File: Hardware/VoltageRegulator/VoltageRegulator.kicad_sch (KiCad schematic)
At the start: 9 parts, among them J1 Conn_01x04, U1 TPS7A2501DRVR

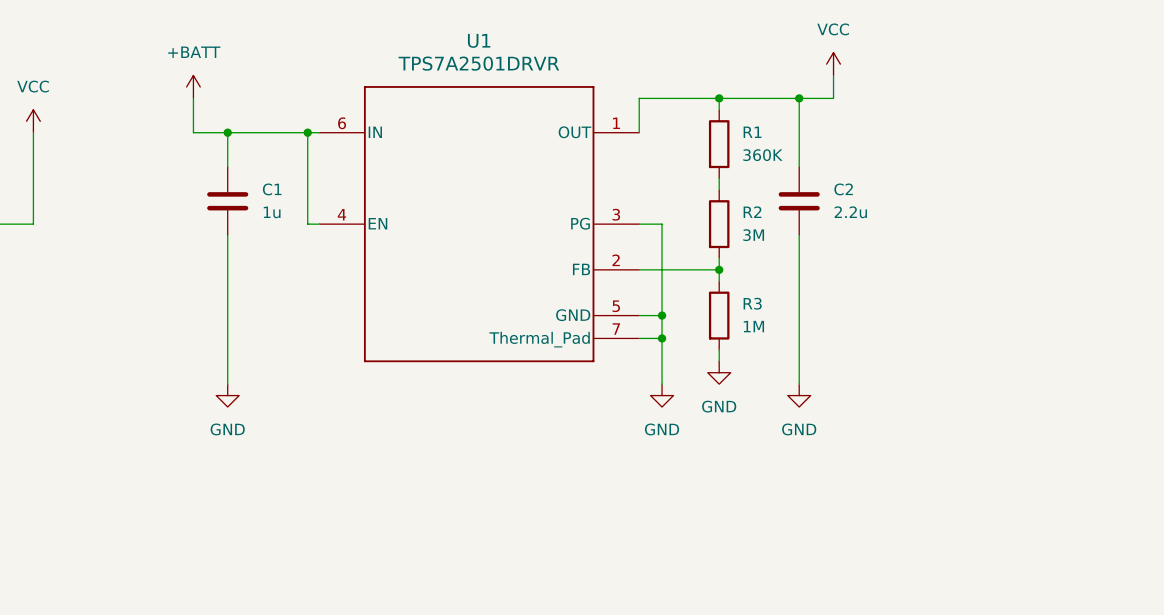
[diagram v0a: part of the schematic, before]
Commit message: Smaller board with isolated mounting holes
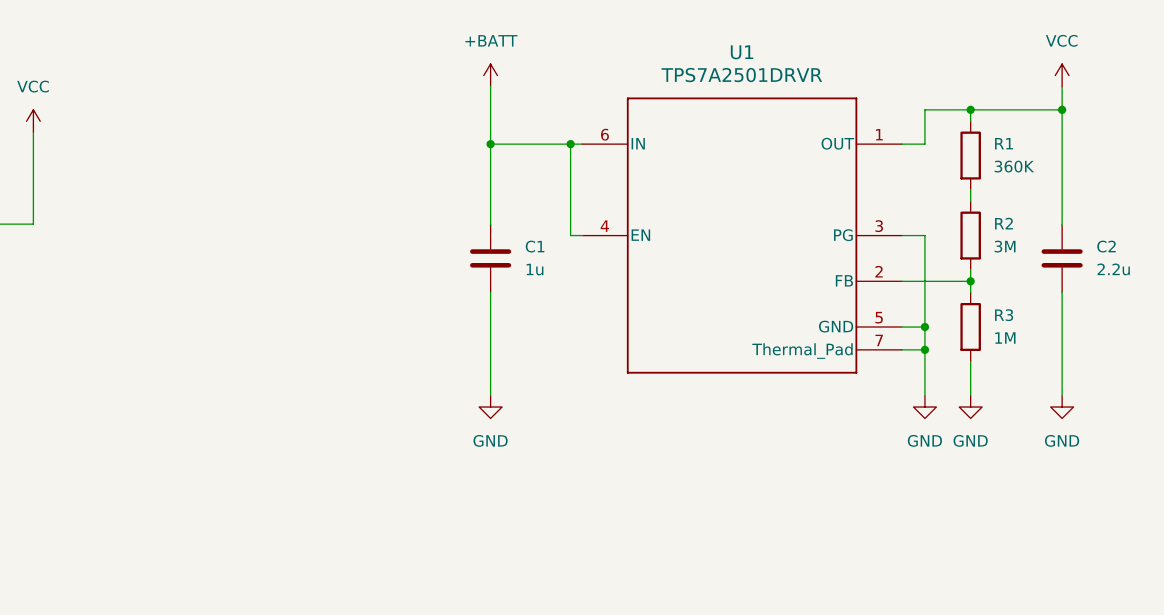
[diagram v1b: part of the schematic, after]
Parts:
- H1, H2: footprint MountingHole:MountingHole_3.2mm_M3 -> MountingHole:MountingHole_3.5mm
- U1: footprint TPS7A2501:DRV0006A-MFG -> TPS7A2501:DRV0006A-IPC_C
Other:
- company: (none) -> Clough42 LLC
- title: (none) -> Mercury Battery Replacement
- moved on the sheet: C1, C2, R1, R2, R3, U1

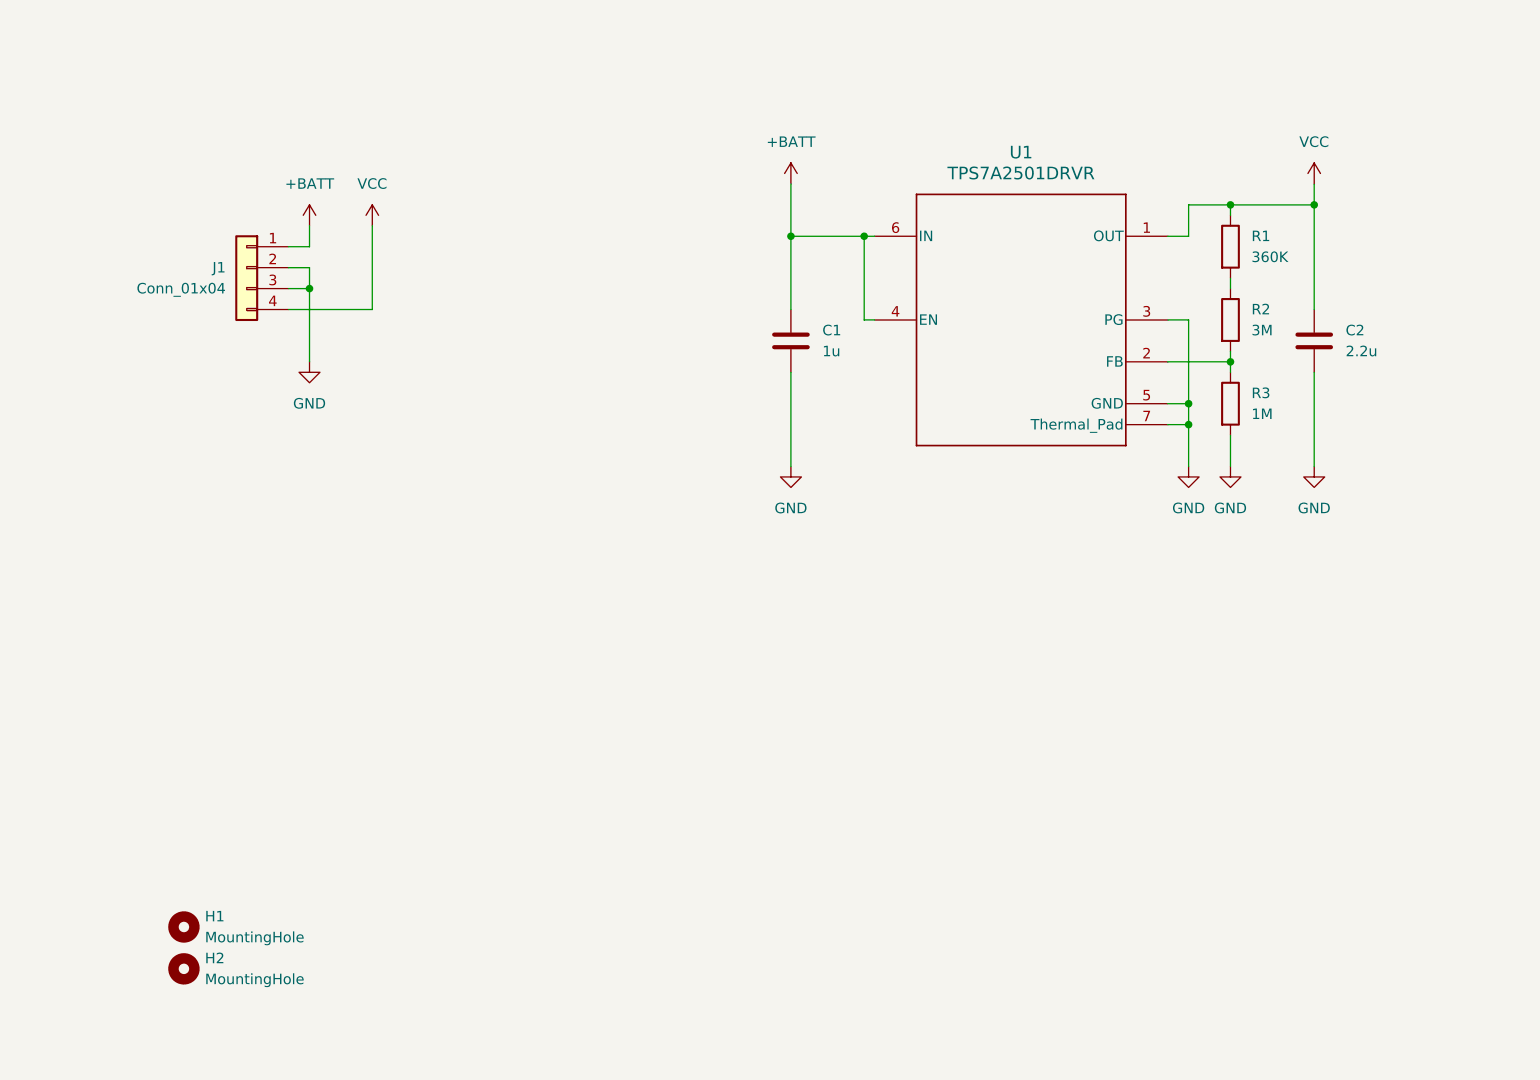
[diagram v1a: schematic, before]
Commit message: Neaten up schematic, add precision designators for resistors
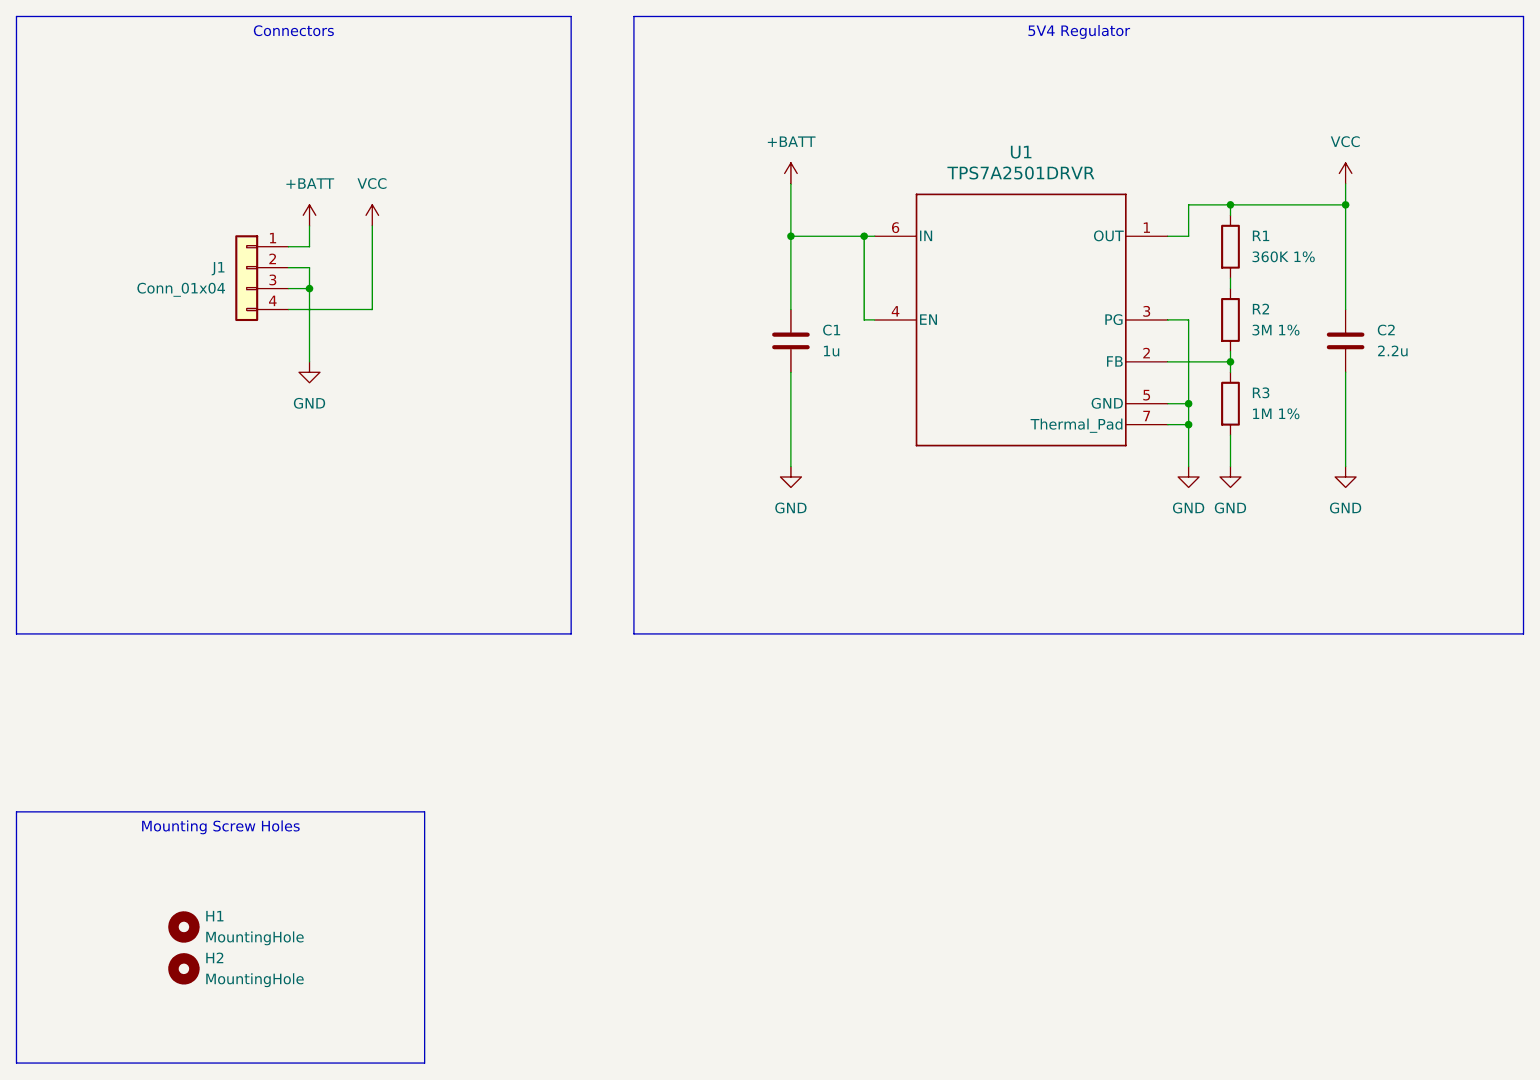
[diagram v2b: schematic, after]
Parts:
- R1: value 360K -> 360K 1%
- R2: value 3M -> 3M 1%
- R3: value 1M -> 1M 1%
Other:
- moved on the sheet: C2
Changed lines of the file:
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@@
     (comment 2 "Low dropout, ultra-low quiescent current")
   )
-  (junction (at 203.2 74.93) (diameter 0) (color 0 0 0 0)
-  )
   (junction (at 193.04 74.93) (diameter 0) (color 0 0 0 0)
   )
@@
   (junction (at 139.7 78.74) (diameter 0) (color 0 0 0 0)
   )
+  (junction (at 207.01 74.93) (diameter 0) (color 0 0 0 0)
+  )
   (wire (pts (xy 185.42 101.6) (xy 187.96 101.6))
     (stroke (width 0) (type default))
@@
     (stroke (width 0) (type default))
   )
-  (wire (pts (xy 193.04 74.93) (xy 203.2 74.93))
-    (stroke (width 0) (type default))
-  )
   (wire (pts (xy 88.9 87.63) (xy 88.9 77.47))
     (stroke (width 0) (type default))
   )
-  (wire (pts (xy 203.2 74.93) (xy 203.2 72.39))
+  (wire (pts (xy 207.01 74.93) (xy 207.01 72.39))
     (stroke (width 0) (type default))
   )
@@
     (stroke (width 0) (type default))
   )
-  (wire (pts (xy 203.2 95.25) (xy 203.2 106.68))
-    (stroke (width 0) (type default))
-  )
   (wire (pts (xy 187.96 74.93) (xy 193.04 74.93))
     (stroke (width 0) (type default))
@@
     (stroke (width 0) (type default))
   )
+  (wire (pts (xy 193.04 74.93) (xy 207.01 74.93))
+    (stroke (width 0) (type default))
+  )
   (wire (pts (xy 185.42 88.9) (xy 187.96 88.9))
     (stroke (width 0) (type default))
@@
     (stroke (width 0) (type default))
   )
-  (wire (pts (xy 203.2 74.93) (xy 203.2 87.63))
+  (wire (pts (xy 207.01 74.93) (xy 207.01 87.63))
     (stroke (width 0) (type default))
   )
@@
     (stroke (width 0) (type default))
   )
+  (wire (pts (xy 207.01 95.25) (xy 207.01 106.68))
+    (stroke (width 0) (type default))
+  )
   (wire (pts (xy 78.74 87.63) (xy 88.9 87.63))
     (stroke (width 0) (type default))
@@
     (stroke (width 0) (type default))
   )
+  (text_box "5V4 Regulator"
+    (at 120.65 52.07 0) (size 107.95 74.93)
+    (stroke (width 0) (type default))
+    (fill (type none))
+    (effects (font (size 1.27 1.27)) (justify top))
+  )
+  (text_box "Mounting Screw Holes"
+    (at 45.72 148.59 0) (size 49.53 30.48)
+    (stroke (width 0) (type default))
+    (fill (type none))
+    (effects (font (size 1.27 1.27)) (justify top))
+  )
+  (text_box "Connectors"
+    (at 45.72 52.07 0) (size 67.31 74.93)
+    (stroke (width 0) (type default))
+    (fill (type none))
+    (effects (font (size 1.27 1.27)) (justify top))
+  )
   (symbol (lib_id "Device:R") (at 193.04 88.9 0) (unit 1)
     (in_bom yes) (on_board yes) (dnp no) (fields_autoplaced)
@@
       (effects (font (size 1.27 1.27)) (justify left))
     )
-    (property "Value" "3M" (at 195.58 90.17 0)
+    (property "Value" "3M 1%" (at 195.58 90.17 0)
       (effects (font (size 1.27 1.27)) (justify left))
     )
@@
     )
   )
-  (symbol (lib_id "power:GND") (at 203.2 106.68 0) (unit 1)
-    (in_bom yes) (on_board yes) (dnp no) (fields_autoplaced)
-    (property "Reference" "#PWR08" (at 203.2 113.03 0)
-      (effects (font (size 1.27 1.27)) hide)
-    )
-    (property "Value" "GND" (at 203.2 111.76 0)
-      (effects (font (size 1.27 1.27)))
-    )
-    (property "Footprint" "" (at 203.2 106.68 0)
-      (effects (font (size 1.27 1.27)) hide)
-    )
-    (property "Datasheet" "" (at 203.2 106.68 0)
+  (symbol (lib_id "power:GND") (at 207.01 106.68 0) (unit 1)
+    (in_bom yes) (on_board yes) (dnp no) (fields_autoplaced)
+    (property "Reference" "#PWR08" (at 207.01 113.03 0)
+      (effects (font (size 1.27 1.27)) hide)
+    )
+    (property "Value" "GND" (at 207.01 111.76 0)
+      (effects (font (size 1.27 1.27)))
+    )
+    (property "Footprint" "" (at 207.01 106.68 0)
+      (effects (font (size 1.27 1.27)) hide)
+    )
+    (property "Datasheet" "" (at 207.01 106.68 0)
       (effects (font (size 1.27 1.27)) hide)
     )
@@
     )
   )
-  (symbol (lib_id "Device:C") (at 203.2 91.44 0) (unit 1)
-    (in_bom yes) (on_board yes) (dnp no) (fields_autoplaced)
-    (property "Reference" "C2" (at 207.01 90.17 0)
-      (effects (font (size 1.27 1.27)) (justify left))
-    )
-    (property "Value" "2.2u" (at 207.01 92.71 0)
-      (effects (font (size 1.27 1.27)) (justify left))
-    )
-    (property "Footprint" "Capacitor_SMD:C_0805_2012Metric" (at 204.1652 95.25 0)
-      (effects (font (size 1.27 1.27)) hide)
-    )
-    (property "Datasheet" "~" (at 203.2 91.44 0)
+  (symbol (lib_id "Device:C") (at 207.01 91.44 0) (unit 1)
+    (in_bom yes) (on_board yes) (dnp no) (fields_autoplaced)
+    (property "Reference" "C2" (at 210.82 90.17 0)
+      (effects (font (size 1.27 1.27)) (justify left))
+    )
+    (property "Value" "2.2u" (at 210.82 92.71 0)
+      (effects (font (size 1.27 1.27)) (justify left))
+    )
+    (property "Footprint" "Capacitor_SMD:C_0805_2012Metric" (at 207.9752 95.25 0)
+      (effects (font (size 1.27 1.27)) hide)
+    )
+    (property "Datasheet" "~" (at 207.01 91.44 0)
       (effects (font (size 1.27 1.27)) hide)
     )
@@
       (effects (font (size 1.27 1.27)) (justify left))
     )
-    (property "Value" "360K" (at 195.58 81.28 0)
+    (property "Value" "360K 1%" (at 195.58 81.28 0)
       (effects (font (size 1.27 1.27)) (justify left))
     )
@@
       (effects (font (size 1.27 1.27)) (justify left))
     )
-    (property "Value" "1M" (at 195.58 100.33 0)
+    (property "Value" "1M 1%" (at 195.58 100.33 0)
       (effects (font (size 1.27 1.27)) (justify left))
     )
@@
     )
   )
-  (symbol (lib_id "power:VCC") (at 203.2 72.39 0) (unit 1)
-    (in_bom yes) (on_board yes) (dnp no) (fields_autoplaced)
-    (property "Reference" "#PWR05" (at 203.2 76.2 0)
-      (effects (font (size 1.27 1.27)) hide)
-    )
-    (property "Value" "VCC" (at 203.2 67.31 0)
-      (effects (font (size 1.27 1.27)))
-    )
-    (property "Footprint" "" (at 203.2 72.39 0)
-      (effects (font (size 1.27 1.27)) hide)
-    )
-    (property "Datasheet" "" (at 203.2 72.39 0)
-      (effects (font (size 1.27 1.27)) hide)
-    )
+  (symbol (lib_id "power:VCC") (at 207.01 72.39 0) (unit 1)
+    (in_bom yes) (on_board yes) (dnp no) (fields_autoplaced)
+    (property "Reference" "#PWR05" (at 207.01 76.2 0)
+      (effects (font (size 1.27 1.27)) hide)
+    )
+    (property "Value" "VCC" (at 207.01 67.31 0)
+      (effects (font (size 1.27 1.27)))
+    )
+    (property "Footprint" "" (at 207.01 72.39 0)
+      (effects (font (size 1.27 1.27)) hide)
+    )
+    (property "Datasheet" "" (at 207.01 72.39 0)
+      (effects (font (size 1.27 1.27)) hide)
+    )

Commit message: Add LCSC part numbers
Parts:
- C1: LCSC Part # (none) -> C28323
- C2: LCSC Part # (none) -> C49217
- R1: LCSC Part # (none) -> C352328
- R2: LCSC Part # (none) -> C269653
- R3: LCSC Part # (none) -> C3016422
- U1: LCSC Part # (none) -> C2864326
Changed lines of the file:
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@@
+      (effects (font (size 1.27 1.27)) hide)
+    )
+    (property "LCSC Part #" "C269653" (at 193.04 88.9 0)
       (effects (font (size 1.27 1.27)) hide)
     )
@@
       (effects (font (size 1.27 1.27)) hide)
     )
+    (property "LCSC Part #" "C49217" (at 207.01 91.44 0)
+      (effects (font (size 1.27 1.27)) hide)
+    )
     (pin "1")
     (pin "2")
@@
     )
     (property "Datasheet" "~" (at 193.04 80.01 0)
+      (effects (font (size 1.27 1.27)) hide)
+    )
+    (property "LCSC Part #" "C352328" (at 193.04 80.01 0)
       (effects (font (size 1.27 1.27)) hide)
     )
@@
     (property "Datasheet" "TPS7A2501DRVR" (at 146.05 74.93 0)
       (effects (font (size 1.27 1.27) italic) hide)
+    )
+    (property "LCSC Part #" "C2864326" (at 149.86 78.74 0)
+      (effects (font (size 1.27 1.27)) hide)
     )
     (pin "3")
@@
       (effects (font (size 1.27 1.27)) hide)
     )
+    (property "LCSC Part #" "C3016422" (at 193.04 99.06 0)
+      (effects (font (size 1.27 1.27)) hide)
+    )
     (pin "1")
     (pin "2")
@@
       (effects (font (size 1.27 1.27)) hide)
     )
+    (property "LCSC Part #" "C28323" (at 139.7 91.44 0)
+      (effects (font (size 1.27 1.27)) hide)
+    )

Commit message: Don't populate header pints
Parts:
- J1: now left out of the parts list
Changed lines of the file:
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@@
   )
   (symbol (lib_id "Connector_Generic:Conn_01x04") (at 73.66 82.55 0) (mirror y) (unit 1)
-    (in_bom yes) (on_board yes) (dnp no)
+    (in_bom no) (on_board yes) (dnp no)
     (property "Reference" "J1" (at 71.12 82.55 0)
       (effects (font (size 1.27 1.27)) (justify left))
